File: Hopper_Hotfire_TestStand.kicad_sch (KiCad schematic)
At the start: 28 parts

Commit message: okokok
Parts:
- BV10, BV11, BV6, BV7, BV8, BV9, Burst_Disc3, CV11, CV12, CV13, Engine2, Needle_Valve2, PT14, PT15, PT16, PT17, PT18, PT19, PT20, Pmatic_B_Valve1, Reg3, SPRV3: value (none) -> ~
- T5: renamed from T1; value (none) -> ~
- T6: renamed from T2; value (none) -> ~
- T7: renamed from T3; value (none) -> ~
- T8: renamed from T4; value (none) -> ~
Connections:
- net at CV11.: now also BV9., PT14., T6.; no longer BV6.
- net at BV11.: now also CV13., nO_Sol8.
- net at PT19.: now also BV10., Engine2.
- net at Pmatic_B_Valve1.: now also BV10.
- net at PT17.: now also Reg3., T7.
- new net: BV6., CV11.
- new net: BV9., Engine2., PT15.
- new net: BV8., Burst_Disc3., CV12., CV13., SPRV3.
- new net: Needle_Valve2., PT20., Pmatic_B_Valve1., T8.
- now unconnected: Burst_Disc3., Engine2., Engine2., PT14., PT15., PT20., SPRV3., T7., T8., nO_Sol8.
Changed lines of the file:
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@@
 	)
 	(symbol
-		(lib_name "PID_symbols:Pressure_Transducer")
 		(lib_id "PID_symbols:Pressure_Transducer")
 		(at 143.51 135.89 0)
@@
 			)
 		)
-		(property "Value" ""
+		(property "Value" "~"
 			(at 143.51 137.16 0)
 			(effects
@@
 	)
 	(symbol
-		(lib_name "PID_symbols:Check_Valve")
 		(lib_id "PID_symbols:Check_Valve")
 		(at 99.06 104.14 0)
@@
 			)
 		)
-		(property "Value" ""
+		(property "Value" "~"
 			(at 99.06 104.14 0)
 			(effects
@@
 	)
 	(symbol
-		(lib_name "PID_symbols:Ball_Valve")
 		(lib_id "PID_symbols:Ball_Valve")
 		(at 49.53 69.85 270)
@@
 			)
 		)
-		(property "Value" ""
+		(property "Value" "~"
 			(at 49.53 69.85 0)
 			(effects
@@
 	)
 	(symbol
-		(lib_name "PID_symbols:Ball_Valve")
 		(lib_id "PID_symbols:Ball_Valve")
 		(at 151.13 85.09 0)
@@
 			)
 		)
-		(property "Value" ""
+		(property "Value" "~"
 			(at 151.13 85.09 0)
 			(effects
@@
 	)
 	(symbol
-		(lib_name "PID_symbols:Ball_Valve")
 		(lib_id "PID_symbols:Ball_Valve")
 		(at 137.16 135.89 90)
@@
 			)
 		)
-		(property "Value" ""
+		(property "Value" "~"
 			(at 137.16 135.89 0)
 			(effects
@@
 	)
 	(symbol
-		(lib_name "PID_symbols:Pressure_Transducer")
 		(lib_id "PID_symbols:Pressure_Transducer")
 		(at 153.67 140.97 0)
@@
 			)
 		)
-		(property "Value" ""
+		(property "Value" "~"
 			(at 153.67 142.24 0)
 			(effects
@@
 			)
 		)
-		(property "Value" ""
+		(property "Value" "~"
 			(at 143.51 147.32 0)
 			(effects
@@
 	)
 	(symbol
-		(lib_name "PID_symbols:Check_Valve")
 		(lib_id "PID_symbols:Check_Valve")
 		(at 140.97 69.85 0)
@@
 			)
 		)
-		(property "Value" ""
+		(property "Value" "~"
 			(at 140.97 69.85 0)
 			(effects
@@
 	)
 	(symbol
-		(lib_name "PID_symbols:Pressure_Transducer")
 		(lib_id "PID_symbols:Pressure_Transducer")
 		(at 132.08 149.86 0)
@@
 			)
 		)
-		(property "Value" ""
+		(property "Value" "~"
 			(at 132.08 151.13 0)
 			(effects
@@
 			)
 		)
-		(property "Value" ""
+		(property "Value" "~"
 			(at 99.06 69.85 0)
 			(effects
@@
 	)
 	(symbol
-		(lib_name "PID_symbols:Pressure_Transducer")
 		(lib_id "PID_symbols:Pressure_Transducer")
 		(at 114.3 114.3 0)
@@
 			)
 		)
-		(property "Value" ""
+		(property "Value" "~"
 			(at 114.3 115.57 0)
 			(effects
@@
 			)
 		)
-		(property "Value" ""
+		(property "Value" "~"
 			(at 181.61 69.85 0)
 			(effects
@@
 	)
 	(symbol
-		(lib_name "PID_symbols:Pressure_Transducer")
 		(lib_id "PID_symbols:Pressure_Transducer")
 		(at 132.08 143.51 0)
@@
 			)
 		)
-		(property "Value" ""
+		(property "Value" "~"
 			(at 132.08 144.78 0)
 			(effects
@@
 	)
 	(symbol
-		(lib_name "PID_symbols:Tank")
 		(lib_id "PID_symbols:Tank")
 		(at 109.22 99.06 0)
@@
 		(on_board yes)
 		(dnp no)
-		(property "Reference" "T2"
+		(property "Reference" "T6"
 			(at 115.57 93.98 0)
 			(effects
@@
 			)
 		)
-		(property "Value" ""
+		(property "Value" "~"
 			(at 109.22 99.06 0)
 			(effects
@@
 			(project "P_IDs"
 				(path "/045f1f05-3134-4b6d-91b6-463031104f1e/12264f82-10ad-4f8b-aee0-7883d457c15c"
-					(reference "T2")
+					(reference "T6")
 					(unit 1)
 				)
@@
 			)
 		)
-		(property "Value" ""
+		(property "Value" "~"
 			(at 110.49 67.31 0)
 			(effects
@@
 			)
 		)
-		(property "Value" ""
+		(property "Value" "~"
 			(at 130.81 59.69 0)
 			(effects
@@
 			)
 		)
-		(property "Value" ""
+		(property "Value" "~"
 			(at 167.64 88.9 0)
 			(effects
@@
 			)
 		)
-		(property "Value" ""
+		(property "Value" "~"
 			(at 175.26 81.28 0)
 			(effects
@@
 	)
 	(symbol
-		(lib_name "PID_symbols:Pressure_Transducer")
 		(lib_id "PID_symbols:Pressure_Transducer")
 		(at 140.97 45.72 0)
@@
 			)
 		)
-		(property "Value" ""
+		(property "Value" "~"
 			(at 140.97 46.99 0)
 			(effects
@@
 			)
 		)
-		(property "Value" ""
+		(property "Value" "~"
 			(at 130.81 57.15 0)
 			(effects
@@
 	)
 	(symbol
-		(lib_name "PID_symbols:Tank")
 		(lib_id "PID_symbols:Tank")
 		(at 129.54 27.94 0)
@@
 		(dnp no)
 		(fields_autoplaced yes)
-		(property "Reference" "T3"
+		(property "Reference" "T7"
 			(at 135.89 23.4949 0)
 			(effects
@@
 			)
 		)
-		(property "Value" ""
+		(property "Value" "~"
 			(at 129.54 27.94 0)
 			(effects
@@
 			(project "P_IDs"
 				(path "/045f1f05-3134-4b6d-91b6-463031104f1e/12264f82-10ad-4f8b-aee0-7883d457c15c"
-					(reference "T3")
-					(unit 1)
-				)
-			)
-		)
-	)
-	(symbol
-		(lib_name "PID_symbols:Ball_Valve")
+					(reference "T7")
+					(unit 1)
+				)
+			)
+		)
+	)
+	(symbol
 		(lib_id "PID_symbols:Ball_Valve")
 		(at 113.03 83.82 0)
@@
 			)
 		)
-		(property "Value" ""
+		(property "Value" "~"
 			(at 113.03 83.82 0)
 			(effects
@@
 			)
 		)
-		(property "Value" ""
+		(property "Value" "~"
 			(at 110.49 72.39 0)
 			(effects
@@
 		(dnp no)
 		(fields_autoplaced yes)
-		(property "Reference" "T1"
+		(property "Reference" "T5"
 			(at 54.61 60.3249 0)
 			(effects
@@
 			)
 		)
-		(property "Value" ""
+		(property "Value" "~"
 			(at 48.26 64.77 0)
 			(effects
@@
 			(project "P_IDs"
 				(path "/045f1f05-3134-4b6d-91b6-463031104f1e/12264f82-10ad-4f8b-aee0-7883d457c15c"
-					(reference "T1")
+					(reference "T5")
 					(unit 1)
 				)
@@
 	)
 	(symbol
-		(lib_name "PID_symbols:Tank")
 		(lib_id "PID_symbols:Tank")
 		(at 166.37 54.61 0)
@@
 		(dnp no)
 		(fields_autoplaced yes)
-		(property "Reference" "T4"
+		(property "Reference" "T8"
 			(at 172.72 50.1649 0)
 			(effects
@@
 			)
 		)
-		(property "Value" ""
+		(property "Value" "~"
 			(at 166.37 54.61 0)
 			(effects
@@
 			(project "P_IDs"
 				(path "/045f1f05-3134-4b6d-91b6-463031104f1e/12264f82-10ad-4f8b-aee0-7883d457c15c"
-					(reference "T4")
-					(unit 1)
-				)
-			)
-		)
-	)
-	(symbol
-		(lib_name "PID_symbols:Ball_Valve")
+					(reference "T8")
+					(unit 1)
+				)
+			)
+		)
+	)
+	(symbol
 		(lib_id "PID_symbols:Ball_Valve")
 		(at 149.86 128.27 270)
@@
 			)
 		)
-		(property "Value" ""
+		(property "Value" "~"
 			(at 149.86 128.27 0)
 			(effects

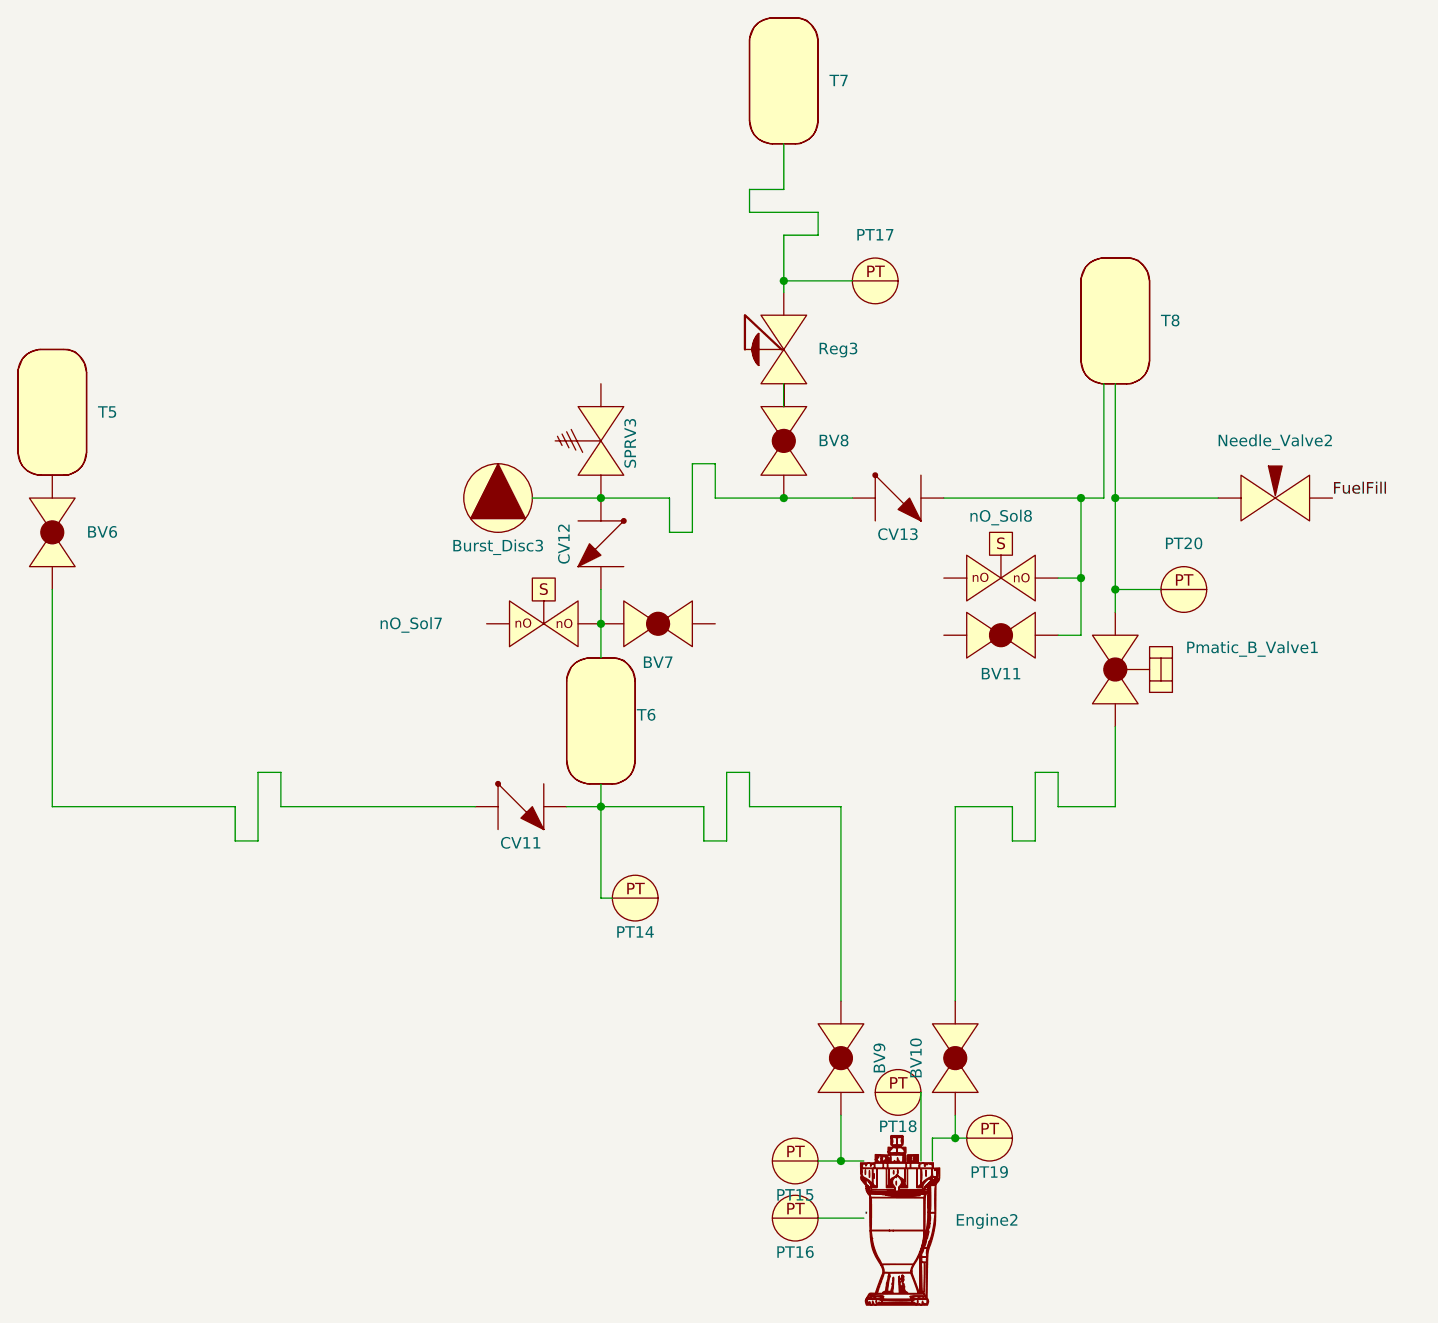
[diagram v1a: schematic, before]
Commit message: Updated igniter PID
+PT +nitrous pressure
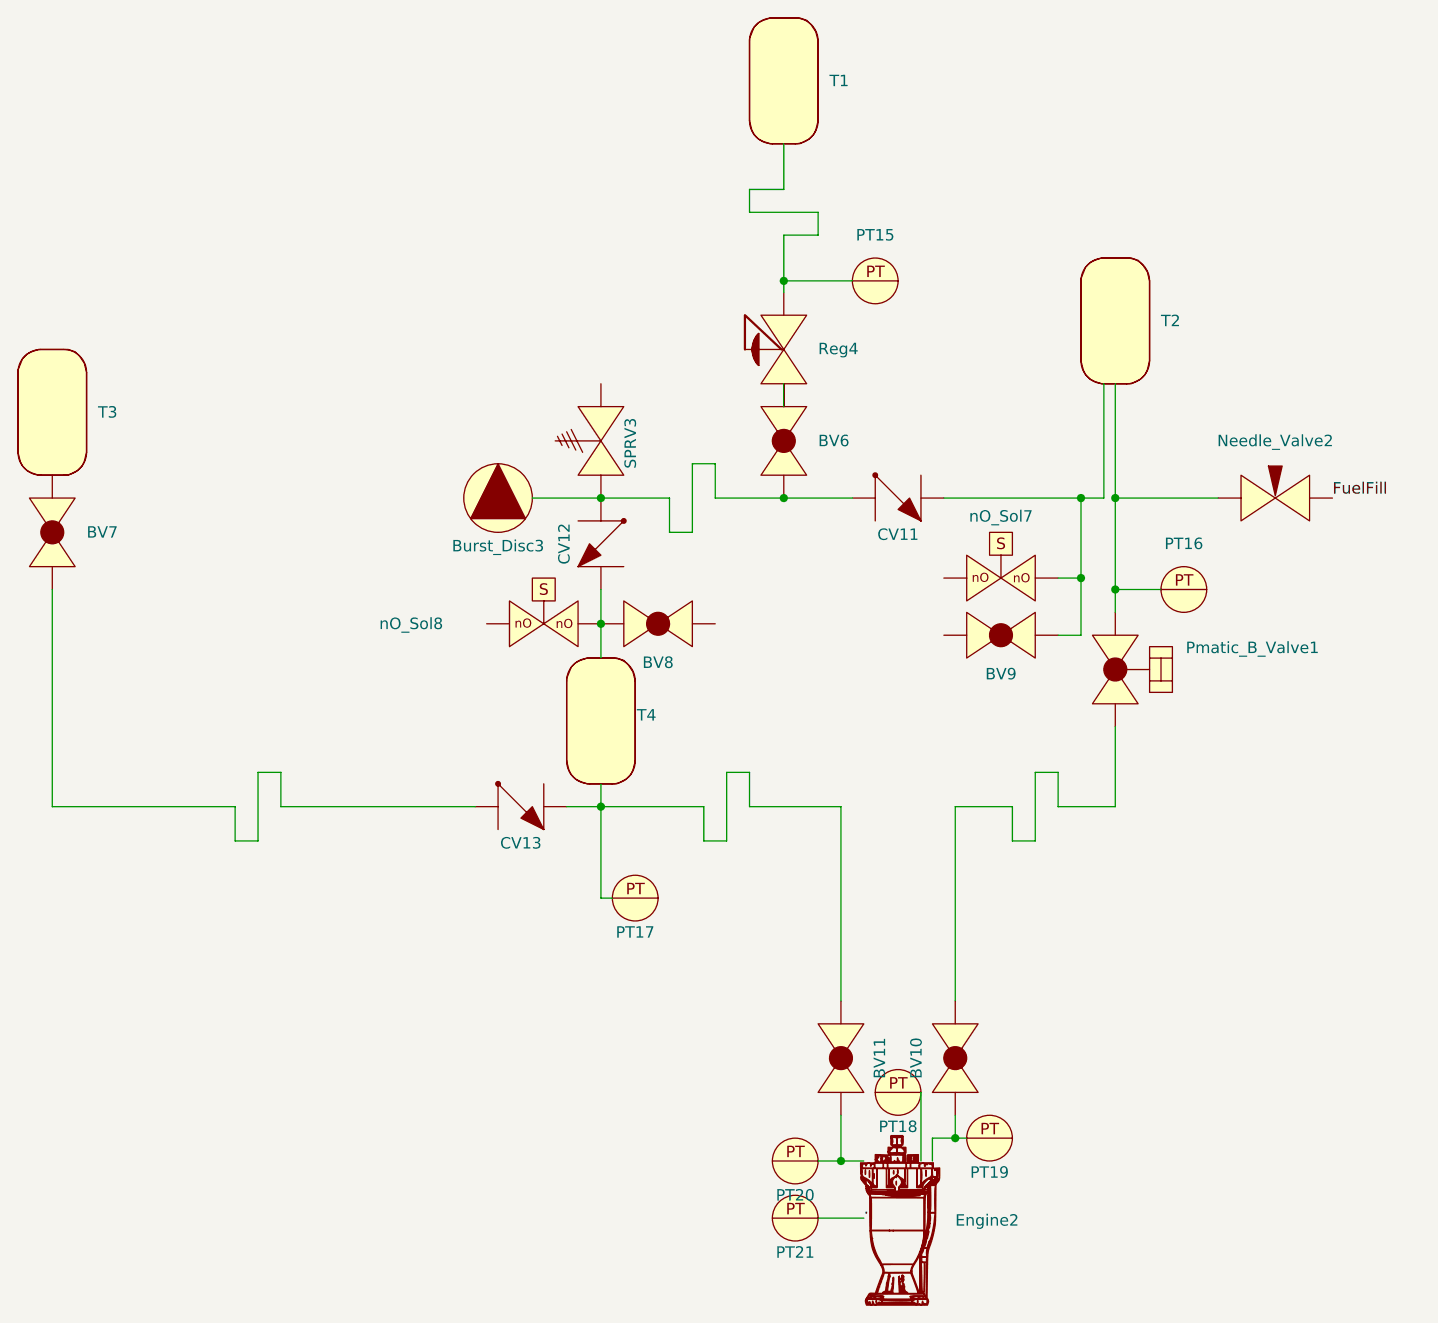
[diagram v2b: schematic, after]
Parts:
- renumbered BV9 to BV11, BV8 to BV6, BV6 to BV7, BV7 to BV8, BV11 to BV9, CV13 to CV11, CV11 to CV13, PT17 to PT15, PT20 to PT16, PT14 to PT17, PT15 to PT20, PT16 to PT21, Reg3 to Reg4, T7 to T1, T8 to T2, T5 to T3, T6 to T4, nO_Sol8 to nO_Sol7, nO_Sol7 to nO_Sol8
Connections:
- net at CV13.: now also BV11., PT17., T4.; no longer BV7.
- net at BV9.: now also CV11., nO_Sol7.
- net at PT19.: now also BV10., Engine2.
- net at Pmatic_B_Valve1.: now also BV10.
- net at PT15.: now also Reg4., T1.
- new net: BV7., CV13.
- new net: BV11., Engine2., PT20.
- new net: BV6., Burst_Disc3., CV11., CV12., SPRV3.
- new net: Needle_Valve2., PT16., Pmatic_B_Valve1., T2.
- now unconnected: Burst_Disc3., Engine2., Engine2., PT16., PT17., PT20., SPRV3., T1., T2., nO_Sol7.
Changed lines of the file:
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@@
 	(label "."
 		(at 139.7 149.86 0)
-		(fields_autoplaced yes)
 		(effects
 			(font
@@
 	(label "FuelFill"
 		(at 191.77 69.85 0)
-		(fields_autoplaced yes)
 		(effects
 			(font
@@
 		(on_board yes)
 		(dnp no)
-		(property "Reference" "CV11"
+		(property "Reference" "CV13"
 			(at 101.6 108.204 0)
 			(effects
@@
 			(project "P_IDs"
 				(path "/045f1f05-3134-4b6d-91b6-463031104f1e/12264f82-10ad-4f8b-aee0-7883d457c15c"
-					(reference "CV11")
+					(reference "CV13")
 					(unit 1)
 				)
@@
 		(dnp no)
 		(fields_autoplaced yes)
-		(property "Reference" "BV6"
+		(property "Reference" "BV7"
 			(at 53.34 73.6599 90)
 			(effects
@@
 			(project "P_IDs"
 				(path "/045f1f05-3134-4b6d-91b6-463031104f1e/12264f82-10ad-4f8b-aee0-7883d457c15c"
-					(reference "BV6")
+					(reference "BV7")
 					(unit 1)
 				)
@@
 		(on_board yes)
 		(dnp no)
-		(property "Reference" "BV11"
+		(property "Reference" "BV9"
 			(at 154.94 89.408 0)
 			(effects
@@
 			(project "P_IDs"
 				(path "/045f1f05-3134-4b6d-91b6-463031104f1e/12264f82-10ad-4f8b-aee0-7883d457c15c"
-					(reference "BV11")
+					(reference "BV9")
 					(unit 1)
 				)
@@
 		(on_board yes)
 		(dnp no)
-		(property "Reference" "BV9"
+		(property "Reference" "BV11"
 			(at 141.478 132.08 0)
 			(effects
@@
 			(project "P_IDs"
 				(path "/045f1f05-3134-4b6d-91b6-463031104f1e/12264f82-10ad-4f8b-aee0-7883d457c15c"
-					(reference "BV9")
+					(reference "BV11")
 					(unit 1)
 				)
@@
 		(on_board yes)
 		(dnp no)
-		(property "Reference" "CV13"
+		(property "Reference" "CV11"
 			(at 143.51 73.914 0)
 			(effects
@@
 			(project "P_IDs"
 				(path "/045f1f05-3134-4b6d-91b6-463031104f1e/12264f82-10ad-4f8b-aee0-7883d457c15c"
-					(reference "CV13")
+					(reference "CV11")
 					(unit 1)
 				)
@@
 		(on_board yes)
 		(dnp no)
-		(property "Reference" "PT16"
+		(property "Reference" "PT21"
 			(at 132.08 153.67 0)
 			(effects
@@
 			(project "P_IDs"
 				(path "/045f1f05-3134-4b6d-91b6-463031104f1e/12264f82-10ad-4f8b-aee0-7883d457c15c"
-					(reference "PT16")
+					(reference "PT21")
 					(unit 1)
 				)
@@
 		(on_board yes)
 		(dnp no)
-		(property "Reference" "nO_Sol8"
+		(property "Reference" "nO_Sol7"
 			(at 154.94 71.882 0)
 			(effects
@@
 			(project "P_IDs"
 				(path "/045f1f05-3134-4b6d-91b6-463031104f1e/12264f82-10ad-4f8b-aee0-7883d457c15c"
-					(reference "nO_Sol8")
+					(reference "nO_Sol7")
 					(unit 1)
 				)
@@
 		(on_board yes)
 		(dnp no)
-		(property "Reference" "PT14"
+		(property "Reference" "PT17"
 			(at 114.3 118.11 0)
 			(effects
@@
 			(project "P_IDs"
 				(path "/045f1f05-3134-4b6d-91b6-463031104f1e/12264f82-10ad-4f8b-aee0-7883d457c15c"
-					(reference "PT14")
+					(reference "PT17")
 					(unit 1)
 				)
@@
 		(on_board yes)
 		(dnp no)
-		(property "Reference" "PT15"
+		(property "Reference" "PT20"
 			(at 132.08 147.32 0)
 			(effects
@@
 			(project "P_IDs"
 				(path "/045f1f05-3134-4b6d-91b6-463031104f1e/12264f82-10ad-4f8b-aee0-7883d457c15c"
-					(reference "PT15")
+					(reference "PT20")
 					(unit 1)
 				)
@@
 		(on_board yes)
 		(dnp no)
-		(property "Reference" "T6"
+		(property "Reference" "T4"
 			(at 115.57 93.98 0)
 			(effects
@@
 			(project "P_IDs"
 				(path "/045f1f05-3134-4b6d-91b6-463031104f1e/12264f82-10ad-4f8b-aee0-7883d457c15c"
-					(reference "T6")
+					(reference "T4")
 					(unit 1)
 				)
@@
 		(dnp no)
 		(fields_autoplaced yes)
-		(property "Reference" "BV8"
+		(property "Reference" "BV6"
 			(at 134.62 63.4999 90)
 			(effects
@@
 			(project "P_IDs"
 				(path "/045f1f05-3134-4b6d-91b6-463031104f1e/12264f82-10ad-4f8b-aee0-7883d457c15c"
-					(reference "BV8")
+					(reference "BV6")
 					(unit 1)
 				)
@@
 		(dnp no)
 		(fields_autoplaced yes)
-		(property "Reference" "PT20"
+		(property "Reference" "PT16"
 			(at 175.26 74.93 0)
 			(effects
@@
 			(project "P_IDs"
 				(path "/045f1f05-3134-4b6d-91b6-463031104f1e/12264f82-10ad-4f8b-aee0-7883d457c15c"
-					(reference "PT20")
+					(reference "PT16")
 					(unit 1)
 				)
@@
 		(dnp no)
 		(fields_autoplaced yes)
-		(property "Reference" "PT17"
+		(property "Reference" "PT15"
 			(at 140.97 40.64 0)
 			(effects
@@
 			(project "P_IDs"
 				(path "/045f1f05-3134-4b6d-91b6-463031104f1e/12264f82-10ad-4f8b-aee0-7883d457c15c"
-					(reference "PT17")
+					(reference "PT15")
 					(unit 1)
 				)
@@
 		(dnp no)
 		(fields_autoplaced yes)
-		(property "Reference" "Reg3"
+		(property "Reference" "Reg4"
 			(at 134.62 53.2774 90)
 			(effects
@@
 			(project "P_IDs"
 				(path "/045f1f05-3134-4b6d-91b6-463031104f1e/12264f82-10ad-4f8b-aee0-7883d457c15c"
-					(reference "Reg3")
+					(reference "Reg4")
 					(unit 1)
 				)
@@
 		(dnp no)
 		(fields_autoplaced yes)
-		(property "Reference" "T7"
+		(property "Reference" "T1"
 			(at 135.89 23.4949 0)
 			(effects
@@
 			(project "P_IDs"
 				(path "/045f1f05-3134-4b6d-91b6-463031104f1e/12264f82-10ad-4f8b-aee0-7883d457c15c"
-					(reference "T7")
+					(reference "T1")
 					(unit 1)
 				)
@@
 		(on_board yes)
 		(dnp no)
-		(property "Reference" "BV7"
+		(property "Reference" "BV8"
 			(at 116.84 88.138 0)
 			(effects
@@
 			(project "P_IDs"
 				(path "/045f1f05-3134-4b6d-91b6-463031104f1e/12264f82-10ad-4f8b-aee0-7883d457c15c"
-					(reference "BV7")
+					(reference "BV8")
 					(unit 1)
 				)
@@
 		(dnp no)
 		(fields_autoplaced yes)
-		(property "Reference" "T5"
+		(property "Reference" "T3"
 			(at 54.61 60.3249 0)
 			(effects
@@
 			(project "P_IDs"
 				(path "/045f1f05-3134-4b6d-91b6-463031104f1e/12264f82-10ad-4f8b-aee0-7883d457c15c"
-					(reference "T5")
+					(reference "T3")
 					(unit 1)
 				)
@@
 		(on_board yes)
 		(dnp no)
-		(property "Reference" "nO_Sol7"
+		(property "Reference" "nO_Sol8"
 			(at 89.408 83.82 0)
 			(effects
@@
 			(project "P_IDs"
 				(path "/045f1f05-3134-4b6d-91b6-463031104f1e/12264f82-10ad-4f8b-aee0-7883d457c15c"
-					(reference "nO_Sol7")
+					(reference "nO_Sol8")
 					(unit 1)
 				)
@@
 		(dnp no)
 		(fields_autoplaced yes)
-		(property "Reference" "T8"
+		(property "Reference" "T2"
 			(at 172.72 50.1649 0)
 			(effects
@@
 			(project "P_IDs"
 				(path "/045f1f05-3134-4b6d-91b6-463031104f1e/12264f82-10ad-4f8b-aee0-7883d457c15c"
-					(reference "T8")
-					(unit 1)
-				)
+					(reference "T2")
+					(unit 1)
+				)
